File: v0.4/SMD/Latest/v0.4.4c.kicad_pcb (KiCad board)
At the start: 2 copper layers, 100 x 100 mm, 299 parts, among them IC3 Trig Cond Socket, J1 Conn_01x05, J2 Conn_01x06, J3 Conn_01x02, J4 Conn_02x20_Counter_Clockwise, J5 Conn_01x04, J6 Conn_01x05, J7 Conn_01x05, J8 Conn_01x03, Q1 SSM3K357R, Q2 SSM3K357R, Q3 SSM3K357R, U1 VNLD5090, U2 TC4424A, U3 VNLD5090, U4 TC4424A, U5 MPX4250, U6 SP720, U7 VNLD5090, U8 LM2940S-5.0/NOPB, U9 VNLD5090

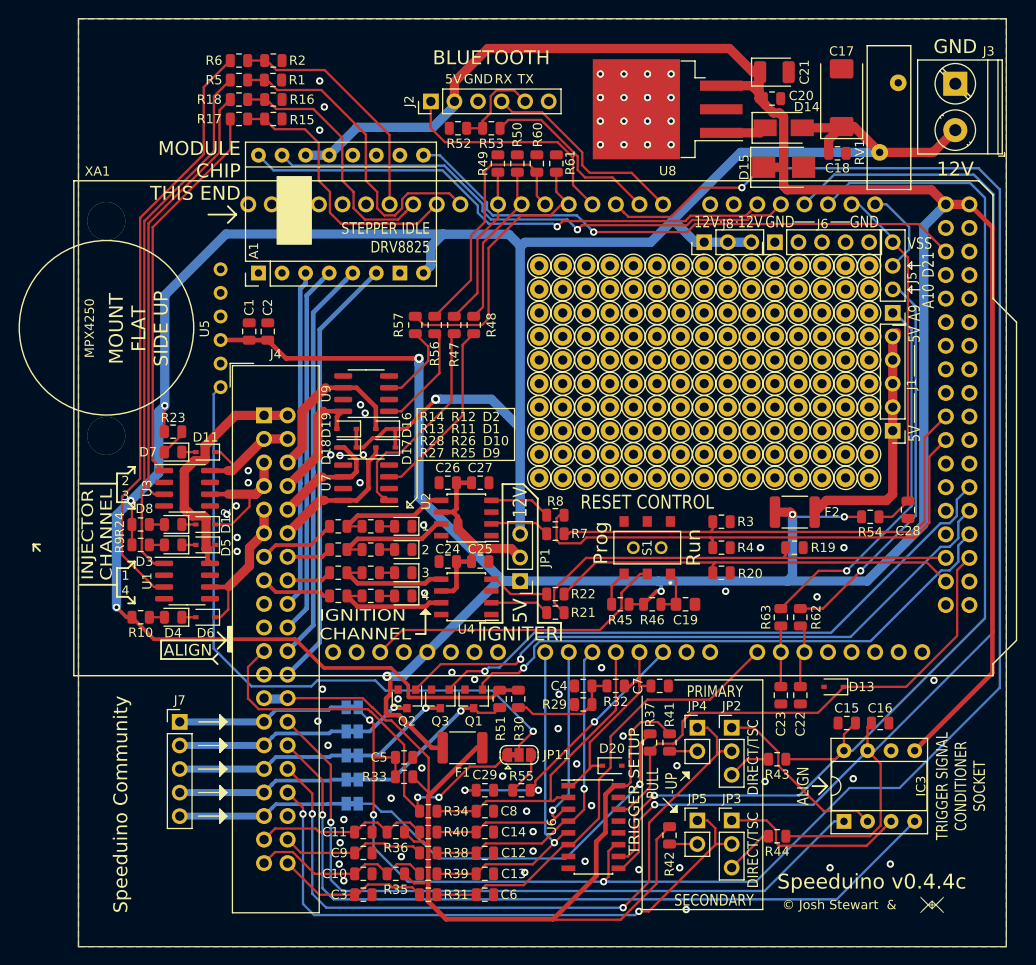
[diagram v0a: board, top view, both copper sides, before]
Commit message: Filled traces
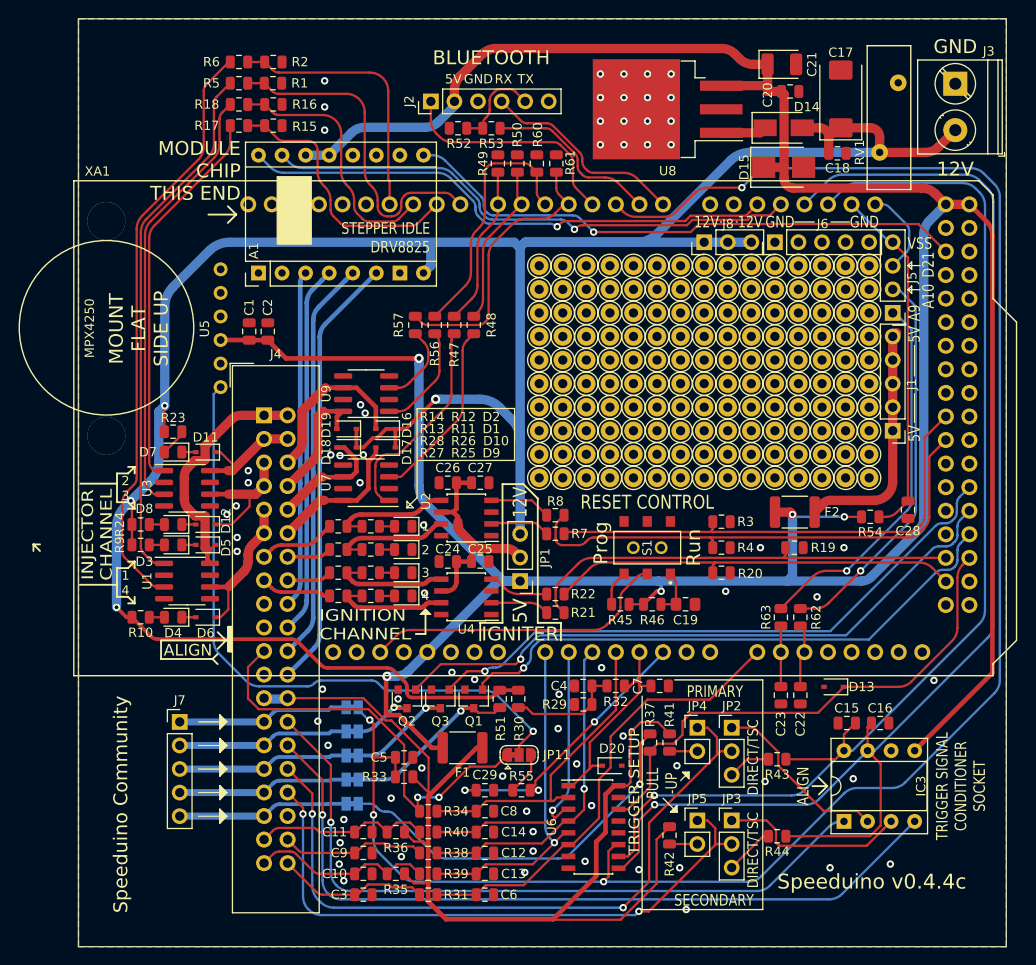
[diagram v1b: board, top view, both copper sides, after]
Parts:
- removed G***: LOGO, Misc:WTM logo_sml
- moved C20 2.09 mm to (187.2, 44.8)
- moved C21 1.17 mm to (186.3, 41.9)
- moved R15 0.71 mm to (131.5, 48.5)
- moved R17 0.71 mm to (127.8, 48.5)
- moved R16 0.53 mm to (131.5, 46.2)
- moved R18 0.53 mm to (127.8, 46.2)
- moved R1 0.34 mm to (131.5, 43.9)
- moved R5 0.34 mm to (127.8, 43.9)
- moved C17 0.16 mm to (192.7, 45.6)
- moved R2 0.16 mm to (131.5, 41.7)
- moved R6 0.16 mm to (127.8, 41.7)
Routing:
- net 12V-SW: track 269.2 -> 281.3 mm
- net MCU-D11: track 26.1 -> 28.9 mm
- net MCU-D8: track 34.9 -> 36.2 mm
- net ADC-Clamp-10: track 201.7 -> 200.5 mm
- net MCU-D1: track 20.0 -> 19.0 mm
- net MCU-D9: track 29.6 -> 28.7 mm
- net Net-(F2-Pad2): track 26.8 -> 26.2 mm
- net Net-(R5-Pad1): track 57.6 -> 57.0 mm
- net Net-(R6-Pad1): track 64.0 -> 63.4 mm
- net MCU-D0: track 22.8 -> 22.3 mm
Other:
- net class Default removed
- board text removed: "© Josh Stewart &"

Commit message: Completed fillet of tracks
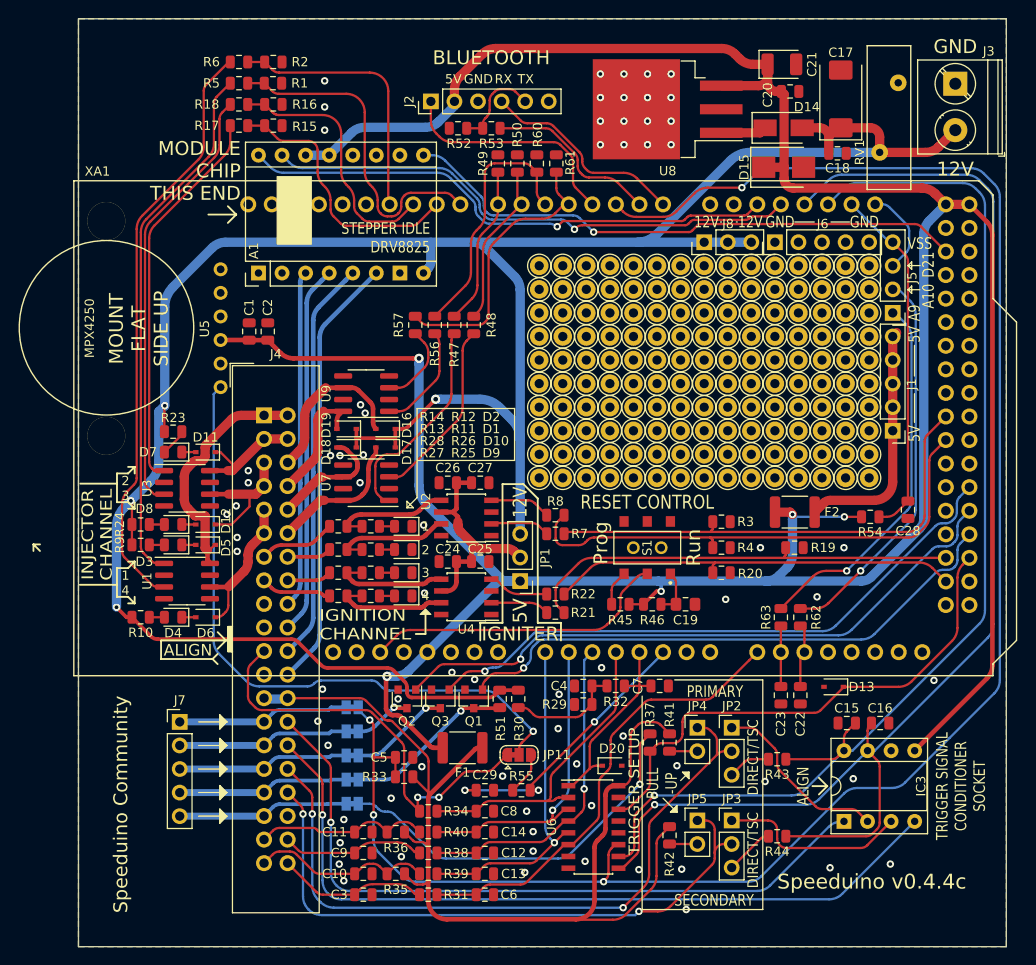
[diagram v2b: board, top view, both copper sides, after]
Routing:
- net 12V-SW: track 281.3 -> 271.0 mm
- net VDD: track 347.1 -> 349.2 mm
- net VDDA: track 136.4 -> 138.0 mm
- net CAM-IN: track 66.5 -> 67.8 mm
- net ADC-Clamp-1: track 23.2 -> 22.0 mm

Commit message: Fixed some issues with v0.4 (SMD)
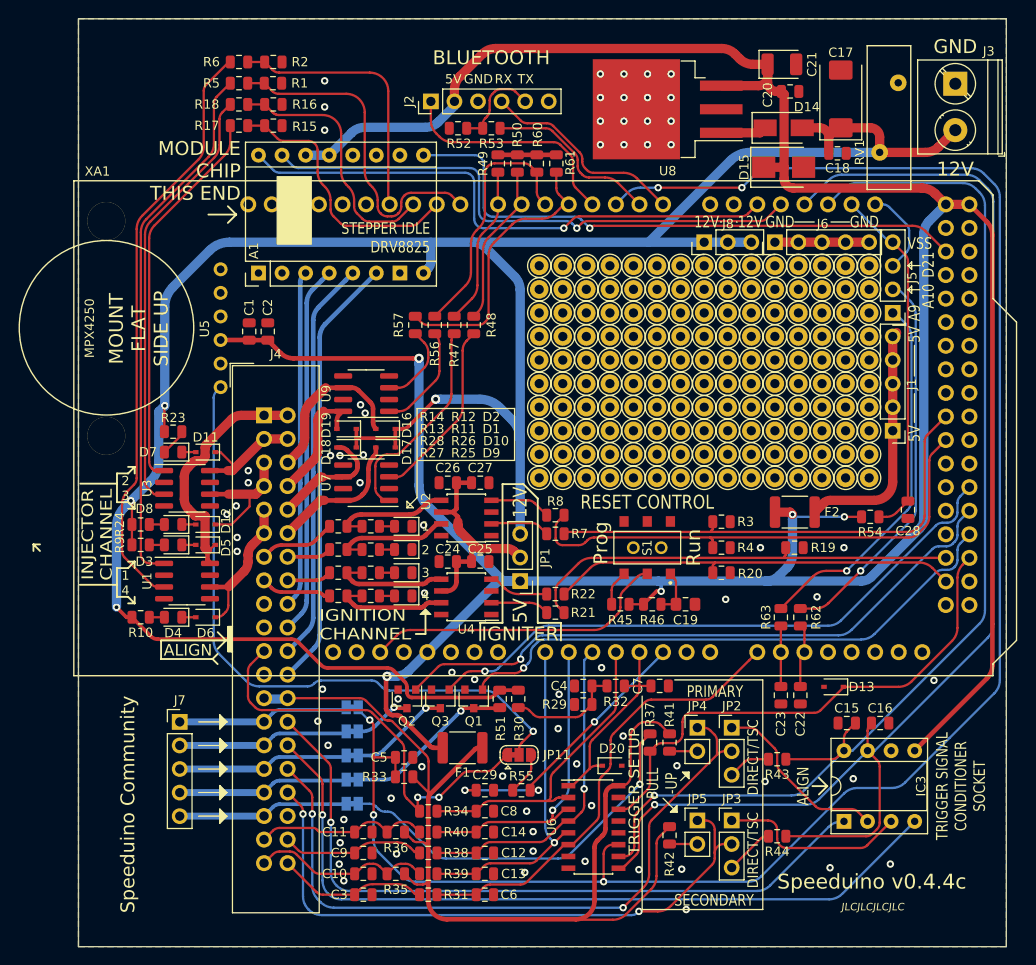
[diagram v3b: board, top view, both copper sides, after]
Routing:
- net GND: track 0.00 -> 16.5 mm
- net MCU-D16: track 58.1 -> 60.5 mm
- net MCU-D17: track 58.3 -> 60.3 mm
- net MCU-D24: track 61.6 -> 63.6 mm
- net 12V-SW: track 271.0 -> 269.9 mm
- net Net-(R5-Pad1): track 57.0 -> 58.1 mm
- net ADC-Clamp-10: track 200.4 -> 199.8 mm, vias 4 -> 5
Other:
- board text added: "JLCJLCJLCJLC"
